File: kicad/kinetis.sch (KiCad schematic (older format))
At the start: 74 parts, among them J1 CONN_01X16, J2 CONN_01X16, J3 CONN_01X16, J4 CONN_01X16, J5 USB_Micro_B, J6 FTDI_Connector, J7 JLink_SWD_20pin, M1 #4-40 Mounting Hole, M2 #4-40 Mounting Hole, M3 #4-40 Mounting Hole, M4 #4-40 Mounting Hole, SW1 SPST, SW2 SPST, SW3 SPST, SW4 SPST, SW5 SPST, SW6 DPDT, U1 MKL16Z64VLH4, U2 LM1117-ADJ, Y1 12.000 MHz

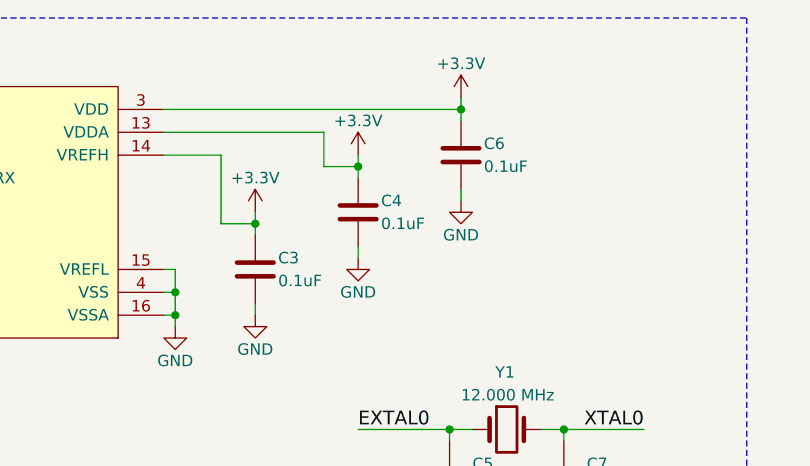
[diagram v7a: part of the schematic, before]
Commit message: Completed analog power. Added extra 22uF cap.
This commit adds another 22uF capacitor to the analog rail, and
also completes the power plane pour.
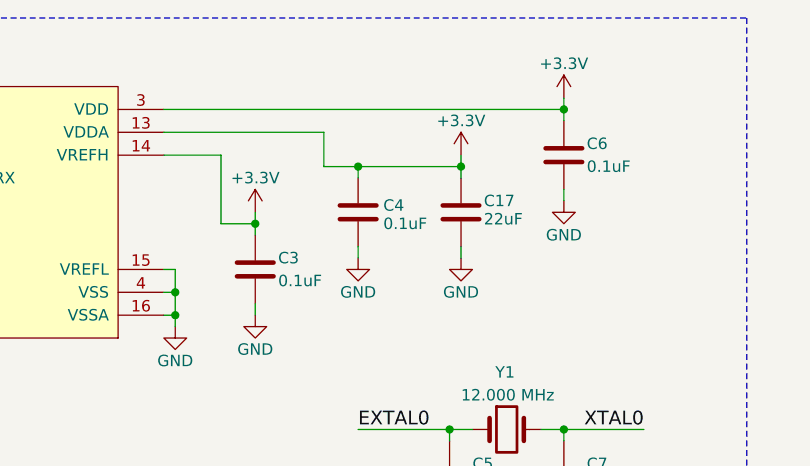
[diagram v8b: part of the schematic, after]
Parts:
- added C17: 22uF, custom_footprints:SM_1206, symbol C
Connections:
- wire segments 312 -> 314
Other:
- moved on the sheet: C6
